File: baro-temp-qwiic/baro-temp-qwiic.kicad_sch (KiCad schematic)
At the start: 4 parts, among them J1 Conn_01x04_Male, U1 BMP388

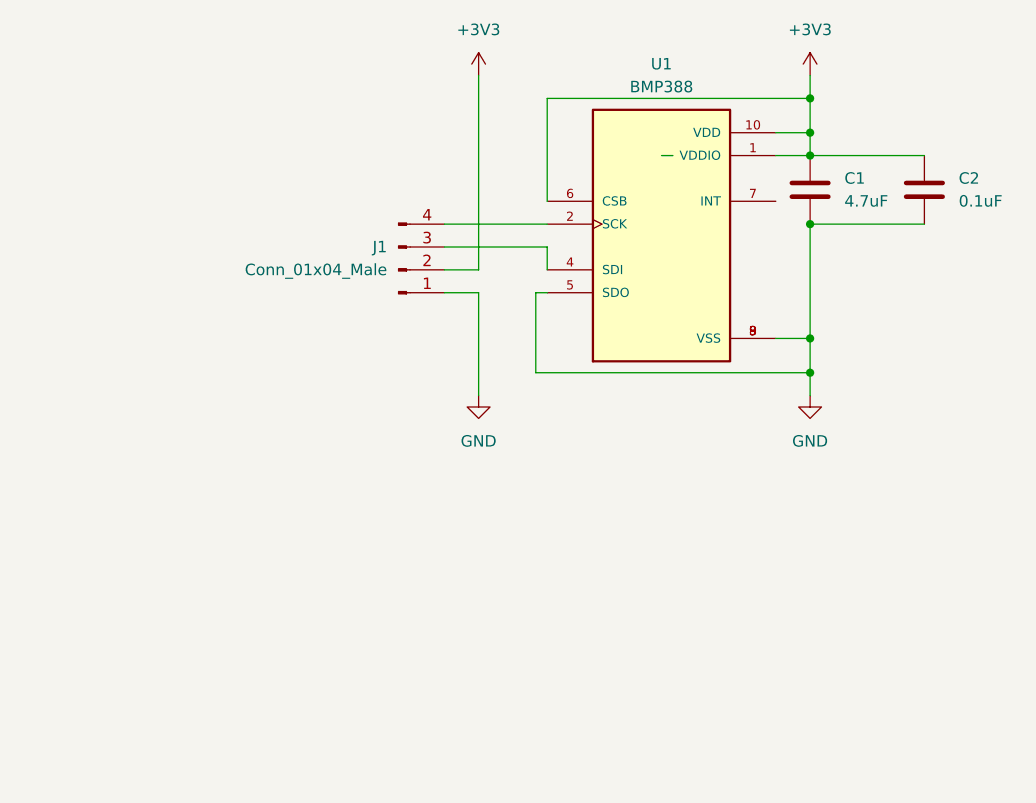
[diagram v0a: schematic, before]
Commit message: Completed pressure-qwiic-3. Completed baro-temp-qwiic. Deleted baro-qwiic.
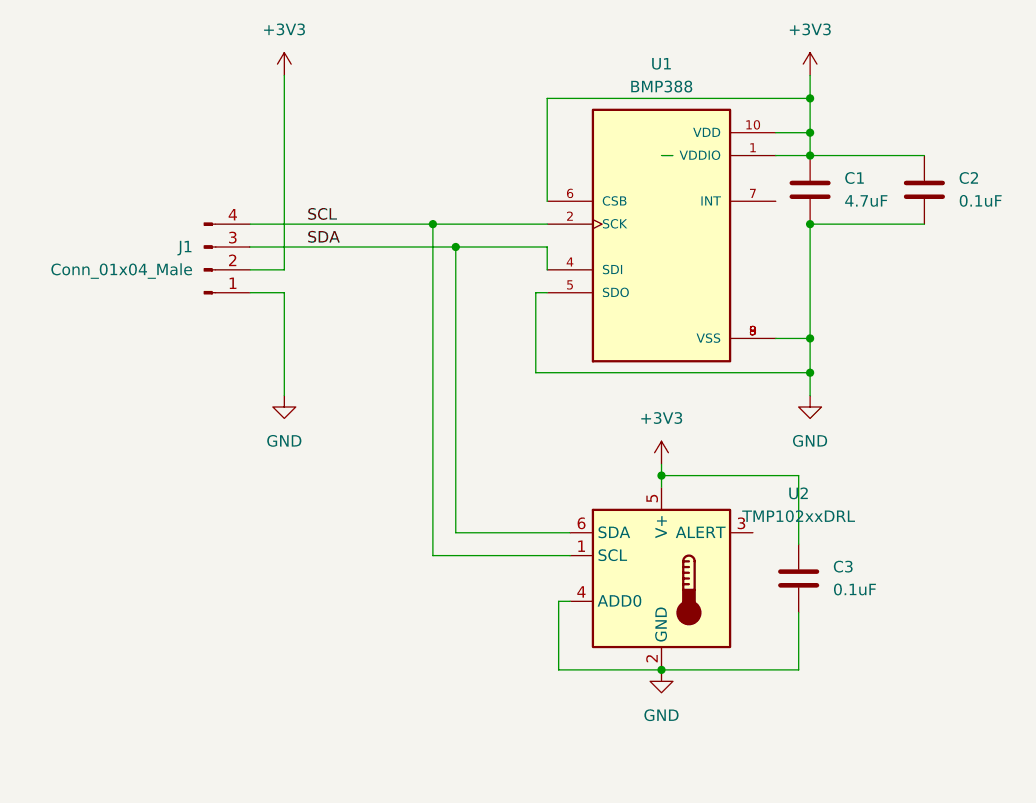
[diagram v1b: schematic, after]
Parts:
- added C3: 0.1uF, Capacitor_SMD:C_0603_1608Metric, symbol Device:C
- added U2: TMP102xxDRL, Package_TO_SOT_SMD:SOT-563, symbol Sensor_Temperature:TMP102xxDRL
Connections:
- net +3V3: now also C3.1, U2.5 (V+)
- net GND: now also C3.2, U2.2 (GND), U2.4 (ADD0)
- net SCL: now reaches J1.4 (Pin_4), U1.2 (SCK)
- net SCL: now also U2.1 (SCL)
- net SDA: now reaches J1.3 (Pin_3), U1.4 (SDI)
- net SDA: now also U2.6 (SDA)
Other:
- moved on the sheet: J1

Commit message: Re-spun board for better solder mask clearance.
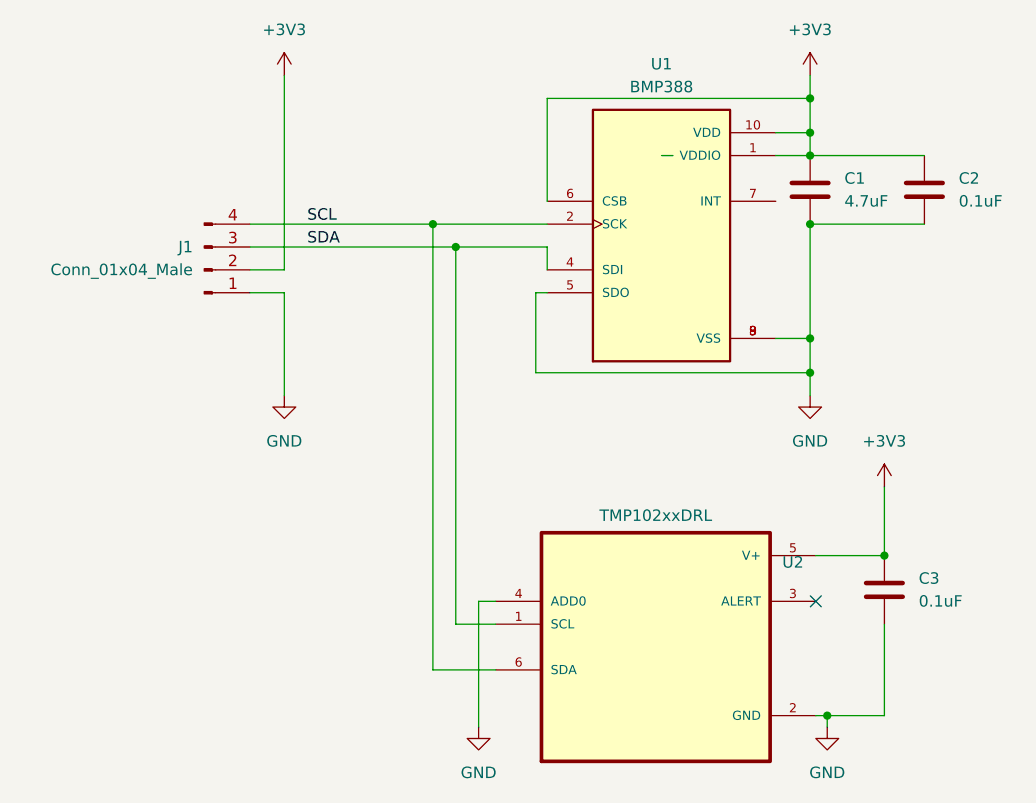
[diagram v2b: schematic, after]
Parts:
- U2: footprint Package_TO_SOT_SMD:SOT-563 -> airball-hardware:TMP102 - SOT50P160X60-6N; symbol Sensor_Temperature:TMP102xxDRL -> airball-hardware:TMP102AIDRLR
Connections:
- net SCL: now also U2.6 (SDA); no longer U2.1 (SCL)
- net SDA: now also U2.1 (SCL); no longer U2.6 (SDA)
- no-connect marks 0 -> 1
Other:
- moved on the sheet: C3
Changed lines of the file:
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@@
   (junction (at 142.24 71.12) (diameter 0) (color 0 0 0 0)
   )
-  (junction (at 125.73 120.65) (diameter 0) (color 0 0 0 0)
+  (junction (at 150.495 107.95) (diameter 0) (color 0 0 0 0)
   )
   (junction (at 142.24 87.63) (diameter 0) (color 0 0 0 0)
@@
   (junction (at 142.24 83.82) (diameter 0) (color 0 0 0 0)
   )
+  (junction (at 144.145 125.73) (diameter 0) (color 0 0 0 0)
+  )
   (junction (at 142.24 60.96) (diameter 0) (color 0 0 0 0)
   )
   (junction (at 100.33 71.12) (diameter 0) (color 0 0 0 0)
   )
-  (junction (at 125.73 99.06) (diameter 0) (color 0 0 0 0)
-  )
-  (wire (pts (xy 125.73 99.06) (xy 140.97 99.06))
+  (no_connect (at 142.875 113.03))
+  (wire (pts (xy 150.495 115.57) (xy 150.495 125.73))
+    (stroke (width 0) (type default) (color 0 0 0 0))
+  )
+  (wire (pts (xy 150.495 125.73) (xy 144.145 125.73))
     (stroke (width 0) (type default) (color 0 0 0 0))
   )
@@
     (stroke (width 0) (type default) (color 0 0 0 0))
   )
+  (wire (pts (xy 150.495 100.33) (xy 150.495 107.95))
+    (stroke (width 0) (type default) (color 0 0 0 0))
+  )
   (wire (pts (xy 142.24 71.12) (xy 142.24 83.82))
     (stroke (width 0) (type default) (color 0 0 0 0))
@@
     (stroke (width 0) (type default) (color 0 0 0 0))
   )
-  (wire (pts (xy 140.97 114.3) (xy 140.97 120.65))
+  (wire (pts (xy 107.315 113.03) (xy 105.41 113.03))
     (stroke (width 0) (type default) (color 0 0 0 0))
   )
@@
     (stroke (width 0) (type default) (color 0 0 0 0))
   )
-  (wire (pts (xy 102.87 105.41) (xy 102.87 73.66))
-    (stroke (width 0) (type default) (color 0 0 0 0))
-  )
   (wire (pts (xy 142.24 87.63) (xy 142.24 90.17))
     (stroke (width 0) (type default) (color 0 0 0 0))
@@
     (stroke (width 0) (type default) (color 0 0 0 0))
   )
-  (wire (pts (xy 140.97 120.65) (xy 125.73 120.65))
+  (wire (pts (xy 142.875 107.95) (xy 150.495 107.95))
     (stroke (width 0) (type default) (color 0 0 0 0))
   )
@@
     (stroke (width 0) (type default) (color 0 0 0 0))
   )
-  (wire (pts (xy 140.97 99.06) (xy 140.97 106.68))
-    (stroke (width 0) (type default) (color 0 0 0 0))
-  )
-  (wire (pts (xy 125.73 99.06) (xy 125.73 100.33))
+  (wire (pts (xy 102.87 115.57) (xy 107.315 115.57))
     (stroke (width 0) (type default) (color 0 0 0 0))
   )
@@
     (stroke (width 0) (type default) (color 0 0 0 0))
   )
-  (wire (pts (xy 100.33 107.95) (xy 100.33 71.12))
+  (wire (pts (xy 100.33 71.12) (xy 100.33 120.65))
+    (stroke (width 0) (type default) (color 0 0 0 0))
+  )
+  (wire (pts (xy 102.87 73.66) (xy 102.87 115.57))
     (stroke (width 0) (type default) (color 0 0 0 0))
   )
@@
     (stroke (width 0) (type default) (color 0 0 0 0))
   )
-  (wire (pts (xy 115.57 105.41) (xy 102.87 105.41))
-    (stroke (width 0) (type default) (color 0 0 0 0))
-  )
-  (wire (pts (xy 114.3 113.03) (xy 114.3 120.65))
-    (stroke (width 0) (type default) (color 0 0 0 0))
-  )
   (wire (pts (xy 142.24 60.96) (xy 138.43 60.96))
     (stroke (width 0) (type default) (color 0 0 0 0))
   )
+  (wire (pts (xy 100.33 120.65) (xy 107.315 120.65))
+    (stroke (width 0) (type default) (color 0 0 0 0))
+  )
   (wire (pts (xy 102.87 73.66) (xy 113.03 73.66))
     (stroke (width 0) (type default) (color 0 0 0 0))
   )
-  (wire (pts (xy 115.57 113.03) (xy 114.3 113.03))
+  (wire (pts (xy 105.41 113.03) (xy 105.41 127))
     (stroke (width 0) (type default) (color 0 0 0 0))
   )
@@
     (stroke (width 0) (type default) (color 0 0 0 0))
   )
-  (wire (pts (xy 100.33 107.95) (xy 115.57 107.95))
-    (stroke (width 0) (type default) (color 0 0 0 0))
-  )
   (wire (pts (xy 111.76 87.63) (xy 142.24 87.63))
     (stroke (width 0) (type default) (color 0 0 0 0))
@@
     (stroke (width 0) (type default) (color 0 0 0 0))
   )
-  (wire (pts (xy 114.3 120.65) (xy 125.73 120.65))
+  (wire (pts (xy 144.145 125.73) (xy 144.145 127))
     (stroke (width 0) (type default) (color 0 0 0 0))
   )
@@
     (stroke (width 0) (type default) (color 0 0 0 0))
   )
-  (wire (pts (xy 125.73 97.79) (xy 125.73 99.06))
+  (wire (pts (xy 142.875 125.73) (xy 144.145 125.73))
     (stroke (width 0) (type default) (color 0 0 0 0))
   )
@@
     (effects (font (size 1.27 1.27)) (justify left bottom))
   )
-  (symbol (lib_id "power:+3V3") (at 125.73 97.79 0) (unit 1)
-    (in_bom yes) (on_board yes) (fields_autoplaced)
-    (property "Reference" "#PWR0102" (id 0) (at 125.73 101.6 0)
-      (effects (font (size 1.27 1.27)) hide)
-    )
-    (property "Value" "+3V3" (id 1) (at 125.73 92.71 0))
-    (property "Footprint" "" (id 2) (at 125.73 97.79 0)
-      (effects (font (size 1.27 1.27)) hide)
-    )
-    (property "Datasheet" "" (id 3) (at 125.73 97.79 0)
+  (symbol (lib_id "power:+3V3") (at 150.495 100.33 0) (unit 1)
+    (in_bom yes) (on_board yes) (fields_autoplaced)
+    (property "Reference" "#PWR0102" (id 0) (at 150.495 104.14 0)
+      (effects (font (size 1.27 1.27)) hide)
+    )
+    (property "Value" "+3V3" (id 1) (at 150.495 95.25 0))
+    (property "Footprint" "" (id 2) (at 150.495 100.33 0)
+      (effects (font (size 1.27 1.27)) hide)
+    )
+    (property "Datasheet" "" (id 3) (at 150.495 100.33 0)
       (effects (font (size 1.27 1.27)) hide)
     )
@@
     (pin "1")
   )
-  (symbol (lib_id "Sensor_Temperature:TMP102xxDRL") (at 125.73 110.49 0) (unit 1)
-    (in_bom yes) (on_board yes) (fields_autoplaced)
-    (property "Reference" "U2" (id 0) (at 140.97 101.0793 0))
-    (property "Value" "TMP102xxDRL" (id 1) (at 140.97 103.6193 0))
-    (property "Footprint" "Package_TO_SOT_SMD:SOT-563" (id 2) (at 127 119.38 0)
-      (effects (font (size 1.27 1.27)) (justify left) hide)
-    )
-    (property "Datasheet" "https://www.ti.com/lit/ds/symlink/tmp102.pdf" (id 3) (at 127 121.92 0)
-      (effects (font (size 1.27 1.27)) (justify left) hide)
+  (symbol (lib_id "power:GND") (at 105.41 127 0) (unit 1)
+    (in_bom yes) (on_board yes) (fields_autoplaced)
+    (property "Reference" "#PWR?" (id 0) (at 105.41 133.35 0)
+      (effects (font (size 1.27 1.27)) hide)
+    )
+    (property "Value" "GND" (id 1) (at 105.41 132.08 0))
+    (property "Footprint" "" (id 2) (at 105.41 127 0)
+      (effects (font (size 1.27 1.27)) hide)
+    )
+    (property "Datasheet" "" (id 3) (at 105.41 127 0)
+      (effects (font (size 1.27 1.27)) hide)
+    )
+    (pin "1")
+  )
+  (symbol (lib_id "airball-hardware:TMP102AIDRLR") (at 125.095 118.11 0) (unit 1)
+    (in_bom yes) (on_board yes)
+    (property "Reference" "U2" (id 0) (at 140.335 108.6993 0))
+    (property "Value" "TMP102xxDRL" (id 1) (at 125.095 103.505 0))
+    (property "Footprint" "airball-hardware:TMP102 - SOT50P160X60-6N" (id 2) (at 125.095 118.11 0)
+      (effects (font (size 1.27 1.27)) (justify left bottom) hide)
+    )
+    (property "Datasheet" "https://www.ti.com/lit/ds/symlink/tmp102.pdf" (id 3) (at 125.095 118.11 0)
+      (effects (font (size 1.27 1.27)) (justify left bottom) hide)
     )
     (pin "1")
@@
     (pin "1")
   )
-  (symbol (lib_id "Device:C") (at 140.97 110.49 0) (unit 1)
-    (in_bom yes) (on_board yes) (fields_autoplaced)
-    (property "Reference" "C3" (id 0) (at 144.78 109.2199 0)
-      (effects (font (size 1.27 1.27)) (justify left))
-    )
-    (property "Value" "0.1uF" (id 1) (at 144.78 111.7599 0)
-      (effects (font (size 1.27 1.27)) (justify left))
-    )
-    (property "Footprint" "Capacitor_SMD:C_0603_1608Metric" (id 2) (at 141.9352 114.3 0)
-      (effects (font (size 1.27 1.27)) hide)
-    )
-    (property "Datasheet" "~" (id 3) (at 140.97 110.49 0)
-      (effects (font (size 1.27 1.27)) hide)
-    )
-    (pin "1")
-    (pin "2")
-  )
-  (symbol (lib_id "power:GND") (at 125.73 120.65 0) (unit 1)
-    (in_bom yes) (on_board yes) (fields_autoplaced)
-    (property "Reference" "#PWR0101" (id 0) (at 125.73 127 0)
-      (effects (font (size 1.27 1.27)) hide)
-    )
-    (property "Value" "GND" (id 1) (at 125.73 125.73 0))
-    (property "Footprint" "" (id 2) (at 125.73 120.65 0)
-      (effects (font (size 1.27 1.27)) hide)
-    )
-    (property "Datasheet" "" (id 3) (at 125.73 120.65 0)
+  (symbol (lib_id "Device:C") (at 150.495 111.76 0) (unit 1)
+    (in_bom yes) (on_board yes) (fields_autoplaced)
+    (property "Reference" "C3" (id 0) (at 154.305 110.4899 0)
+      (effects (font (size 1.27 1.27)) (justify left))
+    )
+    (property "Value" "0.1uF" (id 1) (at 154.305 113.0299 0)
+      (effects (font (size 1.27 1.27)) (justify left))
+    )
+    (property "Footprint" "Capacitor_SMD:C_0603_1608Metric" (id 2) (at 151.4602 115.57 0)
+      (effects (font (size 1.27 1.27)) hide)
+    )
+    (property "Datasheet" "~" (id 3) (at 150.495 111.76 0)
+      (effects (font (size 1.27 1.27)) hide)
+    )
+    (pin "1")
+    (pin "2")
+  )
+  (symbol (lib_id "power:GND") (at 144.145 127 0) (unit 1)
+    (in_bom yes) (on_board yes) (fields_autoplaced)
+    (property "Reference" "#PWR0101" (id 0) (at 144.145 133.35 0)
+      (effects (font (size 1.27 1.27)) hide)
+    )
+    (property "Value" "GND" (id 1) (at 144.145 132.08 0))
+    (property "Footprint" "" (id 2) (at 144.145 127 0)
+      (effects (font (size 1.27 1.27)) hide)
+    )
+    (property "Datasheet" "" (id 3) (at 144.145 127 0)
       (effects (font (size 1.27 1.27)) hide)
     )
@@
       (reference "#PWR0102") (unit 1) (value "+3V3") (footprint "")
     )
+    (path "/538cb2ec-0009-4d1c-9b50-7741dfd303a5"
+      (reference "#PWR?") (unit 1) (value "GND") (footprint "")
+    )
     (path "/23f549d5-7330-4a85-b287-cf75ce373ffc"
       (reference "C1") (unit 1) (value "4.7uF") (footprint "Capacitor_SMD:C_0603_1608Metric")
@@
     )
     (path "/5b246fff-759e-4d50-9a6c-c29c59281bc3"
-      (reference "U2") (unit 1) (value "TMP102xxDRL") (footprint "Package_TO_SOT_SMD:SOT-563")
-    )
-  )
+      (reference "U2") (unit 1) (value "TMP102xxDRL") (footprint "airball-hardware:TMP102 - SOT50P160X60-6N")
+    )
+  )
